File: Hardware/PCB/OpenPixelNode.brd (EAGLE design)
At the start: 100 x 80 mm, 26 parts, among them IC1 wiz820io, IC2 MEGA8-P, IC4 LD117AV33, Q1 20MHz

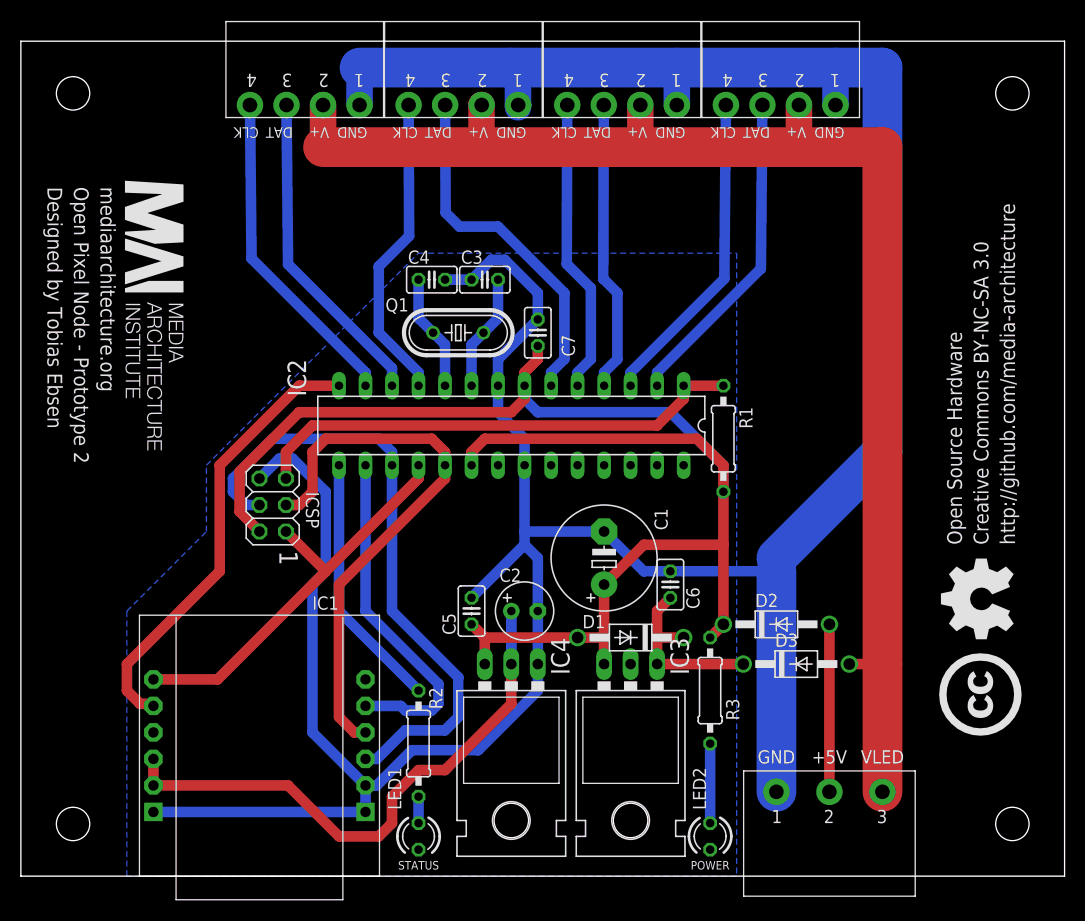
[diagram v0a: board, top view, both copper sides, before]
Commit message: Updated hardware to Prototype 3
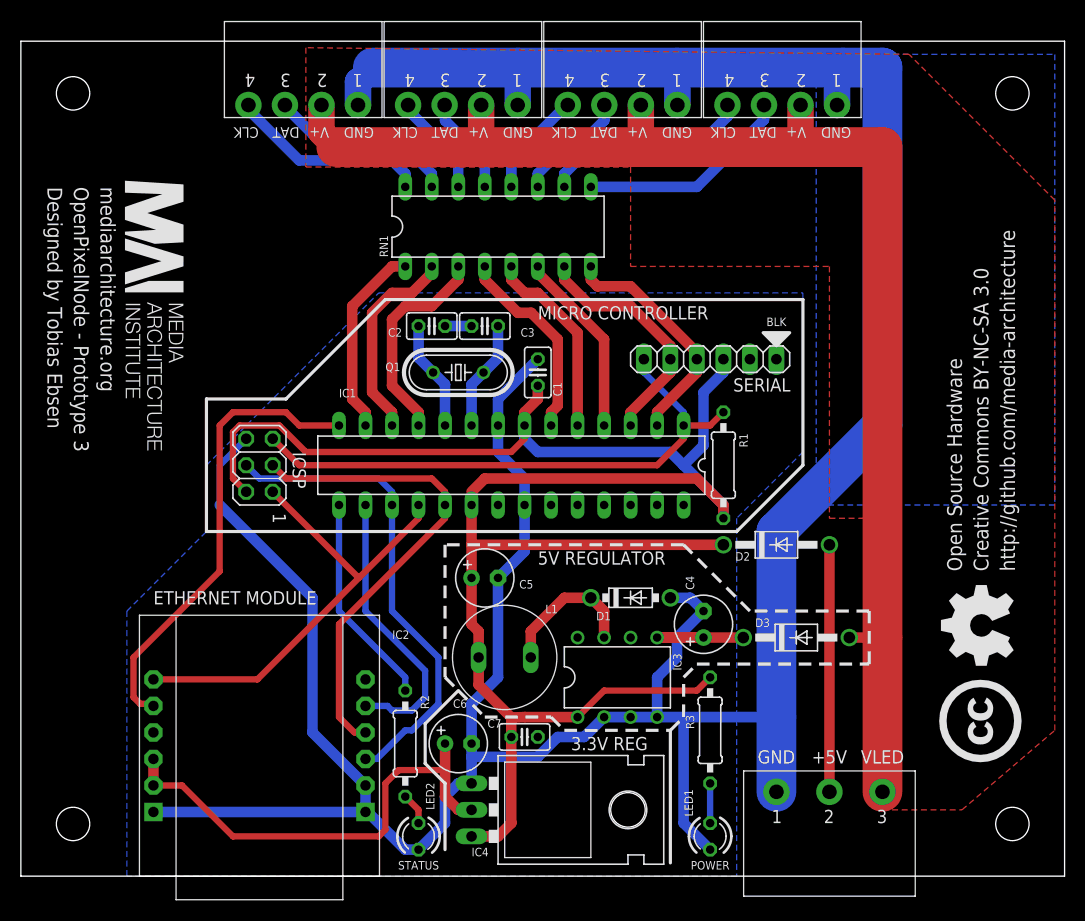
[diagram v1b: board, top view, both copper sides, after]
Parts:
- added L1: 330uH, inductors:13R334C
- added RN1: (no value), resistor-dil:DIL16
- added SERIAL: (no value), pinhead:1X06
- C1: value (none) -> 100nF; device rcl:E5-10,5 -> rcl:C025-025X050
- C2: value (none) -> 22pF; device rcl:E2,5-6 -> rcl:C025-025X050
- C4: value 22pF -> 22uF; device rcl:C025-025X050 -> rcl:E2,5-6
- C5: value (none) -> 220uF; device rcl:C025-025X050 -> rcl:E2,5-6
- C6: value (none) -> 10uF; device rcl:C025-025X050 -> rcl:E2,5-6
- D1: value 1N4004 -> 1N5819-T; device diode:DO41-10 -> diode:DO41-7.6
- IC1: value wiz820io -> MEGA8-P; device Wiz820io:WIZ820IO -> atmel:DIL28-3
- IC2: value MEGA8-P -> wiz820io; device atmel:DIL28-3 -> Wiz820io:WIZ820IO
- IC3: value (none) -> LM2574N-5.0; device v-reg:78XXL -> linear:DIL08
- R2, R3: value (none) -> 220R
- moved C4 42.0 mm to (65.4, 24.1), turned to 90 degrees
- moved IC2 39.0 mm to (22.9, 12.5)
- moved C7 38.8 mm to (48.3, 13.3), turned to 0 degrees
- moved IC1 36.1 mm to (47.0, 39.4)
- moved C2 28.7 mm to (39.4, 52.7), turned to 180 degrees
- moved LED1 27.9 mm to (66.0, 3.81)
- moved LED2 27.9 mm to (38.1, 3.81)
- moved C6 25.4 mm to (41.9, 12.7), turned to 0 degrees
- moved C1 18.9 mm to (49.5, 48.3)
- moved IC4 10.2 mm to (47.0, 6.35), turned to 270 degrees
- moved D2 7.62 mm to (72.4, 31.8)
- moved C3 4.45 mm to (44.5, 52.7)
- moved ICSP 4.02 mm to (22.9, 39.4)
- moved D1 3.81 mm to (58.4, 26.7), turned to 0 degrees
- moved Q1 3.81 mm to (41.9, 48.3)
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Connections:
- new net N$10: D1.C, IC3.7, L1.P$1
- new net N$13: RN1.11, U$2.3
- new net N$14: RN1.12, U$2.4
- new net N$15: RN1.13, U$3.3
- new net N$16: RN1.14, U$3.4
- new net N$17: RN1.15, U$4.3
- new net N$18: RN1.16, U$4.4
- new net N$19: RN1.10, U$1.4
- new net N$20: RN1.9, U$1.3
- net +3V3: now also C6.+, IC2.J2.2, IC2.J2.3; no longer C2.+, IC1.J2.2, IC1.J2.3
- net +5V: now also C1.1, C5.+, IC1.20, IC1.7, IC3.1, L1.P$2, SERIAL.3; no longer C1.+, C5.1, D1.A, IC2.20, IC2.7, IC3.OUT
- net D0: now also IC1.2, RN1.8, SERIAL.4; no longer IC2.2, U$1.3
- net D1: now also IC1.3, RN1.7, SERIAL.5; no longer IC2.3, U$1.4
- net D2: now also IC1.4, RN1.6; no longer IC2.4, U$2.3
- net D3: now also IC1.5, RN1.5; no longer IC2.5, U$2.4
- net D4: now also IC1.6, RN1.4; no longer IC2.6, U$3.3
- net D5: now also IC1.11, RN1.3; no longer IC2.11, U$3.4
- net D6: now also IC1.12, RN1.2; no longer IC2.12, U$4.3
- net D7: now also IC1.13, RN1.1; no longer IC2.13, U$4.4
- net GND: now also C1.2, C2.1, C4.-, C5.-, C6.-, D1.A, IC1.22, IC1.8, IC2.J1.1, IC2.J1.2, IC2.J2.1, IC2.J2.4, IC3.2, IC3.3, IC3.4, SERIAL.1; no longer C1.-, C2.-, C4.1, C5.2, C6.2, IC1.J1.1, IC1.J1.2, IC1.J2.1, IC2.22, IC2.8, IC3.GND
- net N$1: now also LED1.A; no longer LED2.A
- net N$2: now also IC1.9; no longer IC2.9
- net N$21: now also IC1.14, IC2.J2.5; no longer IC1.J2.5, IC2.14
- net N$22: now also IC1.15; no longer IC2.15
- net N$3: now also C2.2, IC1.10; no longer C4.2, IC2.10
- net N$4: now also IC1.16, IC2.J1.5; no longer IC1.J1.5, IC2.16
- net N$5: now also IC1.18, IC2.J2.6; no longer IC1.J2.6, IC2.18
- net N$7: now also IC1.17, IC2.J1.3; no longer IC1.J1.3, IC2.17
- net N$8: now also LED2.A; no longer LED1.A
- net N$9: now also C4.+, IC3.5; no longer C6.1, D1.C, IC3.IN
- net RESET: now also IC1.1, SERIAL.6; no longer IC2.1
- net SCK: now also IC1.19, IC2.J1.4; no longer IC1.J1.4, IC2.19
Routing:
- net +5V: track 148.2 -> 187.0 mm
- net N$20: track 0.00 -> 20.7 mm
- net N$19: track 0.00 -> 20.3 mm
- net N$18: track 0.00 -> 19.2 mm
- net GND: track 306.1 -> 324.5 mm
- net N$17: track 0.00 -> 18.0 mm
- net D4: track 34.3 -> 19.1 mm
- net N$10: track 0.00 -> 13.9 mm
- net N$7: track 60.3 -> 46.4 mm
- net D7: track 31.4 -> 18.6 mm
- net D6: track 31.0 -> 19.5 mm
- net N$13: track 0.00 -> 11.2 mm
- net N$14: track 0.00 -> 10.1 mm
- net D2: track 28.0 -> 17.9 mm
- net N$16: track 0.00 -> 9.83 mm
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- added copper zone on layer 1, net VCC
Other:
- board text added: "3.3V REG"
- board text added: "5V REGULATOR"
- board text added: "BLK"
- board text added: "ETHERNET MODULE"
- board text added: "MICRO CONTROLLER"
- board text added: "OpenPixelNode - Prototype 3"
- board text removed: "Open Pixel Node - Prototype 2"
